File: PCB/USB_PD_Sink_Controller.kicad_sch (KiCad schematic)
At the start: 26 parts, among them J1 USB_C_Receptacle_PowerOnly_6P, J2 JST_01x02_Socket, U1 STUSB4500QTR, U2 STL6P3LLH6, U3 STL6P3LLH6

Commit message: Added Ground plane and started LDO addition to SCH
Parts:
- added C7: 10μF, Capacitor_SMD:C_0603_1608Metric_Pad1.08x0.95mm_HandSolder, symbol Device:C
- added U5: LM2937xT, Package_TO_SOT_THT:TO-220-3_Vertical, symbol Regulator_Linear:LM2937xT
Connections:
- net GND: now also J2.1 (Pin_1), U5.2 (GND); no longer J2.2 (Pin_2)
- net Vbus: now also U5.1 (VI)
- net at C6.2, D4.1 (K), R6.2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: now also J2.2 (Pin_2); no longer J2.1 (Pin_1)
- net at A1.27 (+5V): now also C7.1
- new net: C7.2, U5.3 (VO)

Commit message: Made the Arduino esp32 and added a diode to prevent reverse voltage
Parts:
- removed C7: 10μF, Capacitor_SMD:C_0603_1608Metric_Pad1.08x0.95mm_HandSolder, symbol Device:C
- removed U5: LM2937xT, Package_TO_SOT_THT:TO-220-3_Vertical, symbol Regulator_Linear:LM2937xT
- added D5: D, Diode_SMD:D_0603_1608Metric_Pad1.05x0.95mm_HandSolder, symbol Device:D
- A1: value Arduino_Nano_v2.x -> Arduino_Nano_ESP32; symbol MCU_Module:Arduino_Nano_v2.x -> MCU_Module:Arduino_Nano_ESP32
- J2: footprint Connector_JST:JST_XH_B2B-XH-AM_1x02_P2.50mm_Vertical -> Connector_JST:JST_XH_B2B-XH-A_1x02_P2.50mm_Vertical
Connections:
- net GND: no longer U1.22 (VSYS)
- net Vbus: now also D5.2 (A)
- net VSYS: now reaches A1.17 (3V3)
- net VSYS: now also U1.22 (VSYS)
- net at A1.30 (VIN): now also D5.1 (K)
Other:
- moved on the sheet: R10, R7, R8, R9

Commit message: Added JST to schem
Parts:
- added J3: JST_01x05_Socket, Connector_JST:JST_XH_B5B-XH-A_1x05_P2.50mm_Vertical, symbol Connector:Conn_01x05_Socket
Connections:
- net GND: now also J3.1 (Pin_1)
- net RESET: now also J3.5 (Pin_5)
- net VDD: no longer R4.2, U2.2 (S), U3.2 (S)
- net VSYS: no longer A1.17 (3V3)
- net ALERT_{PU}: now reaches A1.6 (D3), R8.1
- net ALERT_{PU}: now also J3.4 (Pin_4)
- net SDA_{PU}: now reaches A1.23 (SDA/A4), R10.1
- net SDA_{PU}: now also J3.2 (Pin_2)
- net SCL_{PU}: now reaches A1.24 (SCL/A5), R9.1
- net SCL_{PU}: now also J3.3 (Pin_3)
- new net: R4.2, U2.2 (S), U3.2 (S)
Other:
- note added: "Communication Resistors"
- note added: "JST Connection"
- moved on the sheet: R10, R7, R8, R9

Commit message: VDD input added
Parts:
- J3: symbol Connector:Conn_01x05_Socket -> Connector:Conn_01x06_Socket
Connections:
- net VSYS is gone; now on net 3V3: U1.22 (VSYS)
- net Vbus is gone; now on net VDD: C1.1, D1.1 (K), D3.2 (A), D5.2 (A), J1.A9 (VBUS), J1.B9 (VBUS), R1.1, U2.3 (D)
- net ALERT_{PU}: now also J3.5 (Pin_5); no longer J3.4 (Pin_4)
- net RESET: now also J3.6 (Pin_6); no longer J3.5 (Pin_5)
- net SCL_{PU}: now also J3.4 (Pin_4); no longer J3.3 (Pin_3)
- net SDA_{PU}: now also J3.3 (Pin_3); no longer J3.2 (Pin_2)
- net 3V3: now reaches A1.17 (3V3)
- net 3V3: now also J3.2 (Pin_2)
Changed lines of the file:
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@@
+	)
+	(junction
+		(at 191.77 22.86)
+		(diameter 0)
+		(color 0 0 0 0)
 	)
 	(junction
@@
 	(wire
 		(pts
+			(xy 55.88 161.29) (xy 55.88 163.83)
+		)
+		(stroke
+			(width 0)
+			(type default)
+		)
+	)
+	(wire
+		(pts
 			(xy 243.84 46.99) (xy 243.84 34.29)
 		)
@@
 	(wire
 		(pts
-			(xy 180.34 22.86) (xy 195.58 22.86)
+			(xy 45.72 161.29) (xy 45.72 163.83)
+		)
+		(stroke
+			(width 0)
+			(type default)
+		)
+	)
+	(wire
+		(pts
+			(xy 180.34 22.86) (xy 191.77 22.86)
 		)
 		(stroke
@@
 	(wire
 		(pts
+			(xy 48.26 161.29) (xy 48.26 163.83)
+		)
+		(stroke
+			(width 0)
+			(type default)
+		)
+	)
+	(wire
+		(pts
 			(xy 226.06 124.46) (xy 228.6 124.46)
 		)
@@
 	(wire
 		(pts
+			(xy 191.77 22.86) (xy 191.77 36.83)
+		)
+		(stroke
+			(width 0)
+			(type default)
+		)
+	)
+	(wire
+		(pts
 			(xy 78.74 40.64) (xy 83.82 40.64)
 		)
@@
 	(wire
 		(pts
-			(xy 55.88 161.29) (xy 55.88 163.83)
+			(xy 191.77 22.86) (xy 195.58 22.86)
 		)
 		(stroke
@@
 	(wire
 		(pts
-			(xy 48.26 161.29) (xy 48.26 163.83)
-		)
-		(stroke
-			(width 0)
-			(type default)
-		)
-	)
-	(wire
-		(pts
 			(xy 180.34 22.86) (xy 180.34 26.67)
 		)
@@
 	(wire
 		(pts
+			(xy 73.66 88.9) (xy 72.39 88.9)
+		)
+		(stroke
+			(width 0)
+			(type default)
+		)
+	)
+	(wire
+		(pts
 			(xy 273.05 25.4) (xy 273.05 44.45)
 		)
@@
 	(wire
 		(pts
+			(xy 260.35 109.22) (xy 264.16 109.22)
+		)
+		(stroke
+			(width 0)
+			(type default)
+		)
+	)
+	(wire
+		(pts
+			(xy 229.87 121.92) (xy 228.6 121.92)
+		)
+		(stroke
+			(width 0)
+			(type default)
+		)
+	)
+	(wire
+		(pts
+			(xy 22.86 55.88) (xy 30.48 55.88)
+		)
+		(stroke
+			(width 0)
+			(type default)
+		)
+	)
+	(wire
+		(pts
+			(xy 166.37 22.86) (xy 170.18 22.86)
+		)
+		(stroke
+			(width 0)
+			(type default)
+		)
+	)
+	(wire
+		(pts
+			(xy 30.48 55.88) (xy 33.02 55.88)
+		)
+		(stroke
+			(width 0)
+			(type default)
+		)
+	)
+	(wire
+		(pts
+			(xy 22.86 50.8) (xy 22.86 55.88)
+		)
+		(stroke
+			(width 0)
+			(type default)
+		)
+	)
+	(wire
+		(pts
+			(xy 180.34 43.18) (xy 180.34 46.99)
+		)
+		(stroke
+			(width 0)
+			(type default)
+		)
+	)
+	(wire
+		(pts
+			(xy 45.72 25.4) (xy 49.53 25.4)
+		)
+		(stroke
+			(width 0)
+			(type default)
+		)
+	)
+	(wire
+		(pts
+			(xy 22.86 171.45) (xy 27.94 171.45)
+		)
+		(stroke
+			(width 0)
+			(type default)
+		)
+	)
+	(wire
+		(pts
 			(xy 50.8 161.29) (xy 50.8 163.83)
-		)
-		(stroke
-			(width 0)
-			(type default)
-		)
-	)
-	(wire
-		(pts
-			(xy 260.35 109.22) (xy 264.16 109.22)
-		)
-		(stroke
-			(width 0)
-			(type default)
-		)
-	)
-	(wire
-		(pts
-			(xy 229.87 121.92) (xy 228.6 121.92)
-		)
-		(stroke
-			(width 0)
-			(type default)
-		)
-	)
-	(wire
-		(pts
-			(xy 22.86 55.88) (xy 30.48 55.88)
-		)
-		(stroke
-			(width 0)
-			(type default)
-		)
-	)
-	(wire
-		(pts
-			(xy 166.37 22.86) (xy 170.18 22.86)
-		)
-		(stroke
-			(width 0)
-			(type default)
-		)
-	)
-	(wire
-		(pts
-			(xy 30.48 55.88) (xy 33.02 55.88)
-		)
-		(stroke
-			(width 0)
-			(type default)
-		)
-	)
-	(wire
-		(pts
-			(xy 22.86 50.8) (xy 22.86 55.88)
-		)
-		(stroke
-			(width 0)
-			(type default)
-		)
-	)
-	(wire
-		(pts
-			(xy 180.34 43.18) (xy 180.34 46.99)
-		)
-		(stroke
-			(width 0)
-			(type default)
-		)
-	)
-	(wire
-		(pts
-			(xy 45.72 25.4) (xy 49.53 25.4)
-		)
-		(stroke
-			(width 0)
-			(type default)
-		)
-	)
-	(wire
-		(pts
-			(xy 22.86 171.45) (xy 27.94 171.45)
 		)
 		(stroke
@@
 		)
 	)
+	(label "3V3"
+		(at 73.66 88.9 0)
+		(effects
+			(font
+				(size 1.27 1.27)
+			)
+			(justify left bottom)
+		)
+	)
 	(label "DISCH"
 		(at 243.84 46.99 0)
@@
 		)
 	)
-	(label "VSYS"
+	(label "3V3"
 		(at 245.11 81.28 90)
 		(effects
@@
 	)
 	(label "ALERT_{PU}"
-		(at 50.8 161.29 90)
+		(at 48.26 161.29 90)
 		(effects
 			(font
@@
 	)
 	(label "SCL_{PU}"
-		(at 53.34 161.29 90)
+		(at 50.8 161.29 90)
 		(effects
 			(font
@@
 		)
 	)
+	(label "VDD"
+		(at 191.77 36.83 270)
+		(effects
+			(font
+				(size 1.27 1.27)
+			)
+			(justify right bottom)
+		)
+	)
 	(label "Vbus"
 		(at 34.29 78.74 0)
@@
 		)
 	)
+	(label "3V3"
+		(at 55.88 161.29 90)
+		(effects
+			(font
+				(size 1.27 1.27)
+			)
+			(justify left bottom)
+		)
+	)
 	(label "Vbus"
 		(at 60.96 25.4 0)
@@
 	)
 	(label "SDA_{PU}"
-		(at 55.88 161.29 90)
+		(at 53.34 161.29 90)
 		(effects
 			(font
@@
 	)
 	(label "RESET"
-		(at 48.26 161.29 90)
+		(at 45.72 161.29 90)
 		(effects
 			(font
@@
 	)
 	(symbol
-		(lib_id "Connector:Conn_01x05_Socket")
+		(lib_id "Connector:Conn_01x06_Socket")
 		(at 53.34 168.91 270)
 		(unit 1)
@@
 		(fields_autoplaced yes)
 		(property "Reference" "J3"
-			(at 53.34 171.45 90)
+			(at 52.07 171.45 90)
 			(effects
 				(font
@@
 		)
 		(property "Value" "JST_01x05_Socket"
-			(at 53.34 173.99 90)
+			(at 52.07 173.99 90)
 			(effects
 				(font
@@
 		(pin "3"
 		)
+		(pin "6"
+		)
 		(instances

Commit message: Updated PCB
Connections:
- net ALERT_{PU} is gone; now on net ALERT: A1.6 (D3), J3.5 (Pin_5), R8.1
- net ALERT: no longer R8.2, U1.7 (SCL)
- net GND: now also C3.2, C4.2, C5.2, R7.1; no longer C3.1, C4.1, C5.1, R7.2
- net RESET: now also R7.2; no longer R7.1
- net SCL: now also A1.24 (SCL/A5), J3.4 (Pin_4); no longer U1.19 (ALERT)
- net SDA: now also A1.23 (SDA/A4), J3.3 (Pin_3); no longer U1.8 (SDA)
- net VDD: now also C3.1; no longer C3.2
- net at U1.21 (VREG_1V2): now also C5.1; no longer C5.2
- net at U1.23 (VREG_2V7): now also C4.1; no longer C4.2
- removed net SCL_{PU}: A1.24 (SCL/A5), J3.4 (Pin_4), R9.1
- removed net SDA_{PU}: A1.23 (SDA/A4), J3.3 (Pin_3), R10.1
- new net: R8.2, U1.7 (SCL)
- new net: R9.1, U1.19 (ALERT)
- new net: R10.1, U1.8 (SDA)
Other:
- note removed: "Communication Resistors"
- moved on the sheet: C3, C4, C5, J3, R10, R7, R8, R9

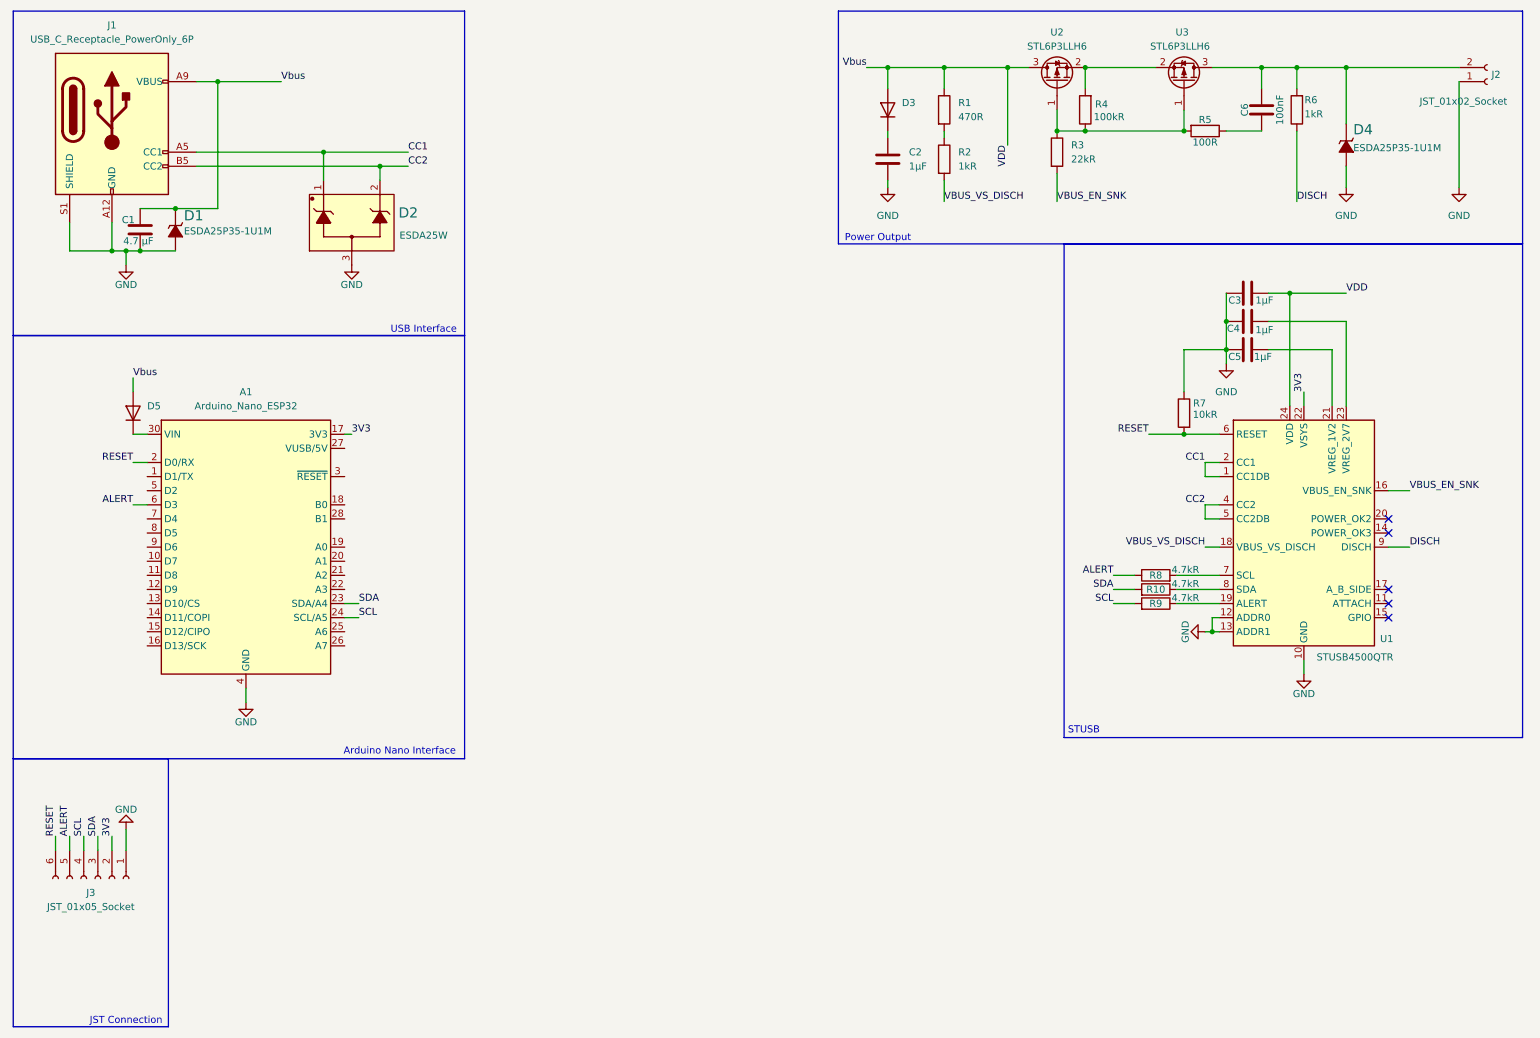
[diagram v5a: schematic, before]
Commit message: Made min VBUS main and added BOM
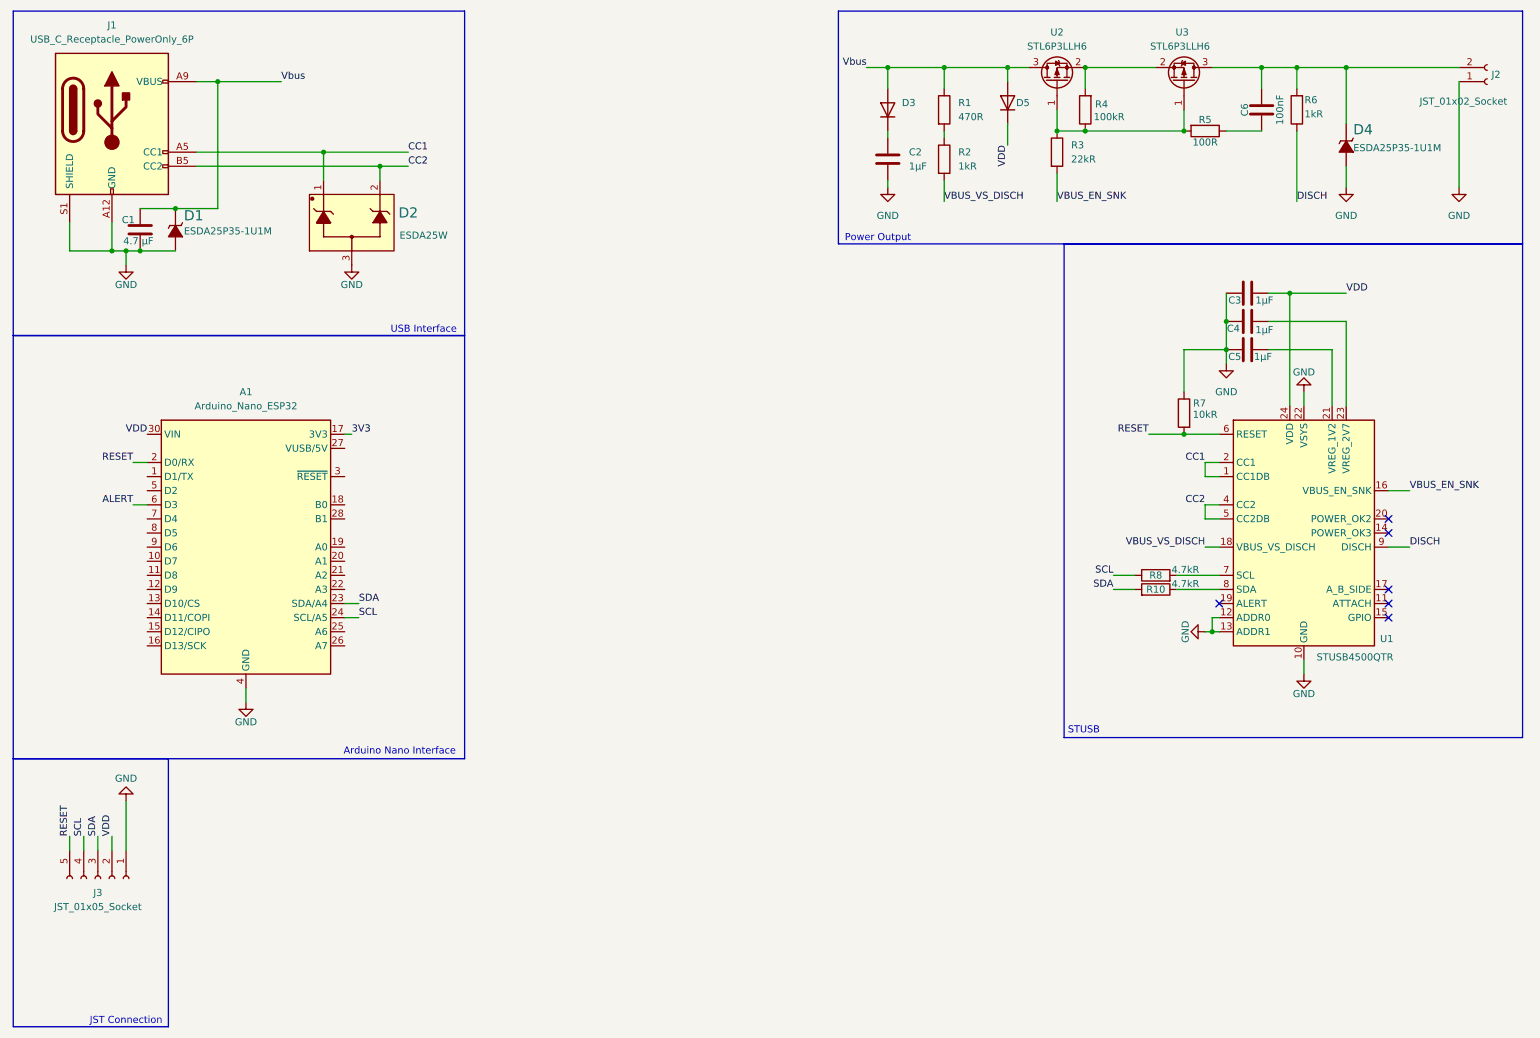
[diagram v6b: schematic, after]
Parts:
- removed R9: 4.7kR, Resistor_SMD:R_0603_1608Metric_Pad0.98x0.95mm_HandSolder, symbol Device:R
- J2: footprint Connector_JST:JST_XH_B2B-XH-A_1x02_P2.50mm_Vertical -> Connector_JST:JST_XH_S2B-XH-A_1x02_P2.50mm_Horizontal
- J3: footprint Connector_JST:JST_XH_B5B-XH-A_1x05_P2.50mm_Vertical -> Connector_JST:JST_XH_S5B-XH-A_1x05_P2.50mm_Horizontal; symbol Connector:Conn_01x06_Socket -> Connector:Conn_01x05_Socket
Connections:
- net 3V3: no longer J3.2 (Pin_2), U1.22 (VSYS)
- net ALERT: no longer J3.5 (Pin_5), R8.1
- net GND: now also U1.22 (VSYS)
- net RESET: now also J3.5 (Pin_5); no longer J3.6 (Pin_6)
- net SCL: now also R8.1
- net VDD: now also A1.30 (VIN), D5.1 (K), J3.2 (Pin_2); no longer C1.1, D1.1 (K), D3.2 (A), D5.2 (A), J1.A9 (VBUS), J1.B9 (VBUS), R1.1, U2.3 (D)
- new net Vbus: C1.1, D1.1 (K), D3.2 (A), D5.2 (A), J1.A9 (VBUS), J1.B9 (VBUS), R1.1, U2.3 (D)
- no-connect marks 5 -> 6
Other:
- company: (none) -> UF FOCUS LAB
- title: (none) -> STUSB-1-0
- moved on the sheet: D5
